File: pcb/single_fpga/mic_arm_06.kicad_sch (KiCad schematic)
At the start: 17 parts, among them U105 CDCLVC1108PW, U49 IM72D128V01XTMA1, U50 IM72D128V01XTMA1, U51 IM72D128V01XTMA1, U52 IM72D128V01XTMA1, U53 IM72D128V01XTMA1, U54 IM72D128V01XTMA1, U55 IM72D128V01XTMA1, U56 IM72D128V01XTMA1

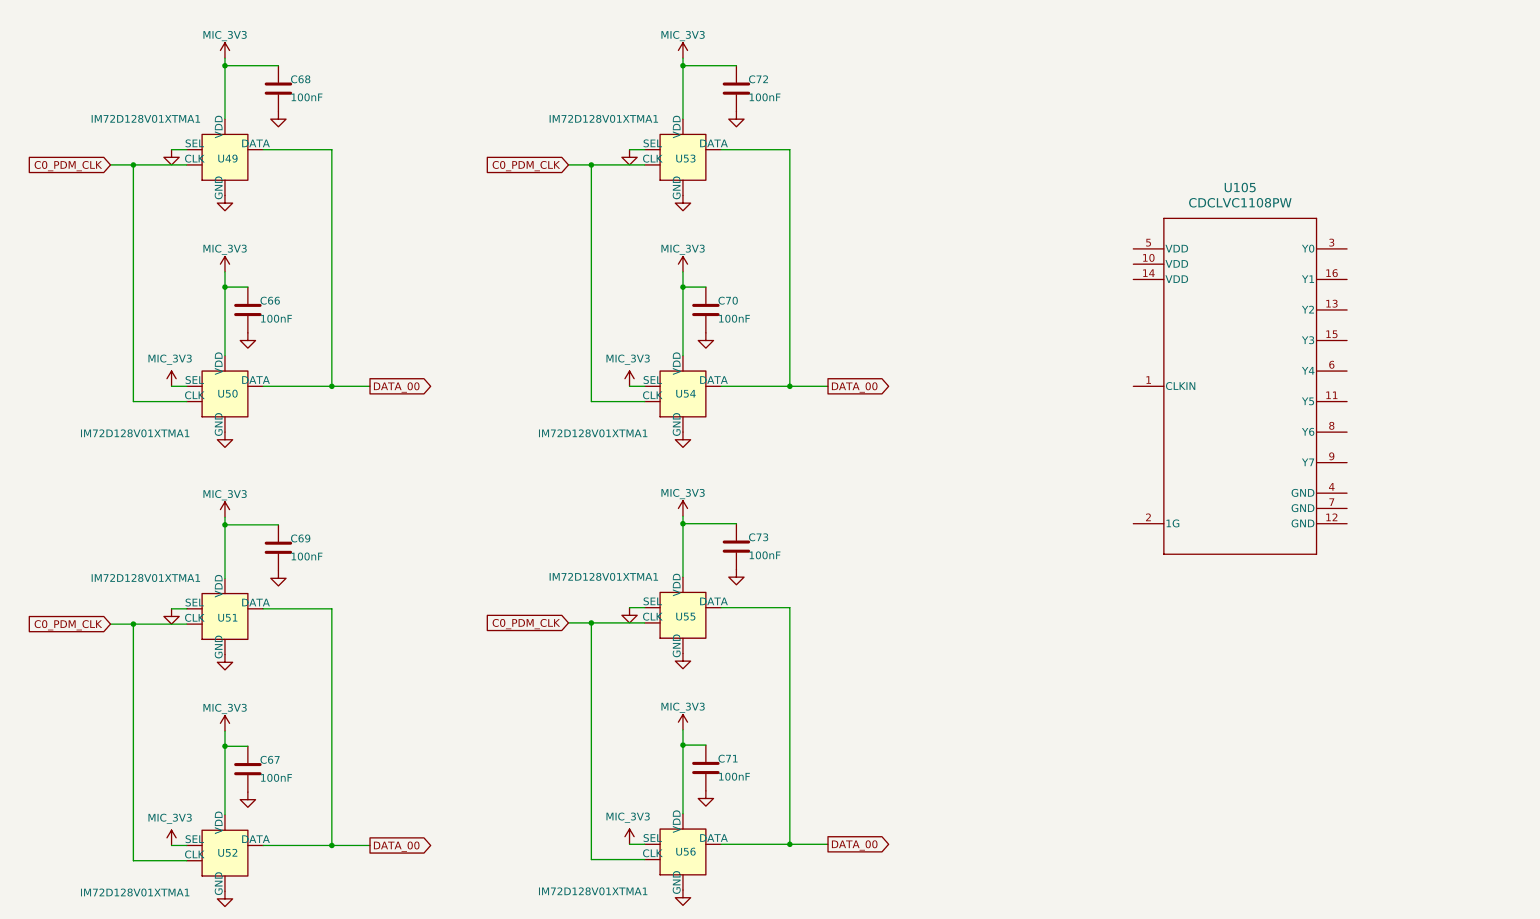
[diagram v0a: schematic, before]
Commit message: Fixed clocks and names.
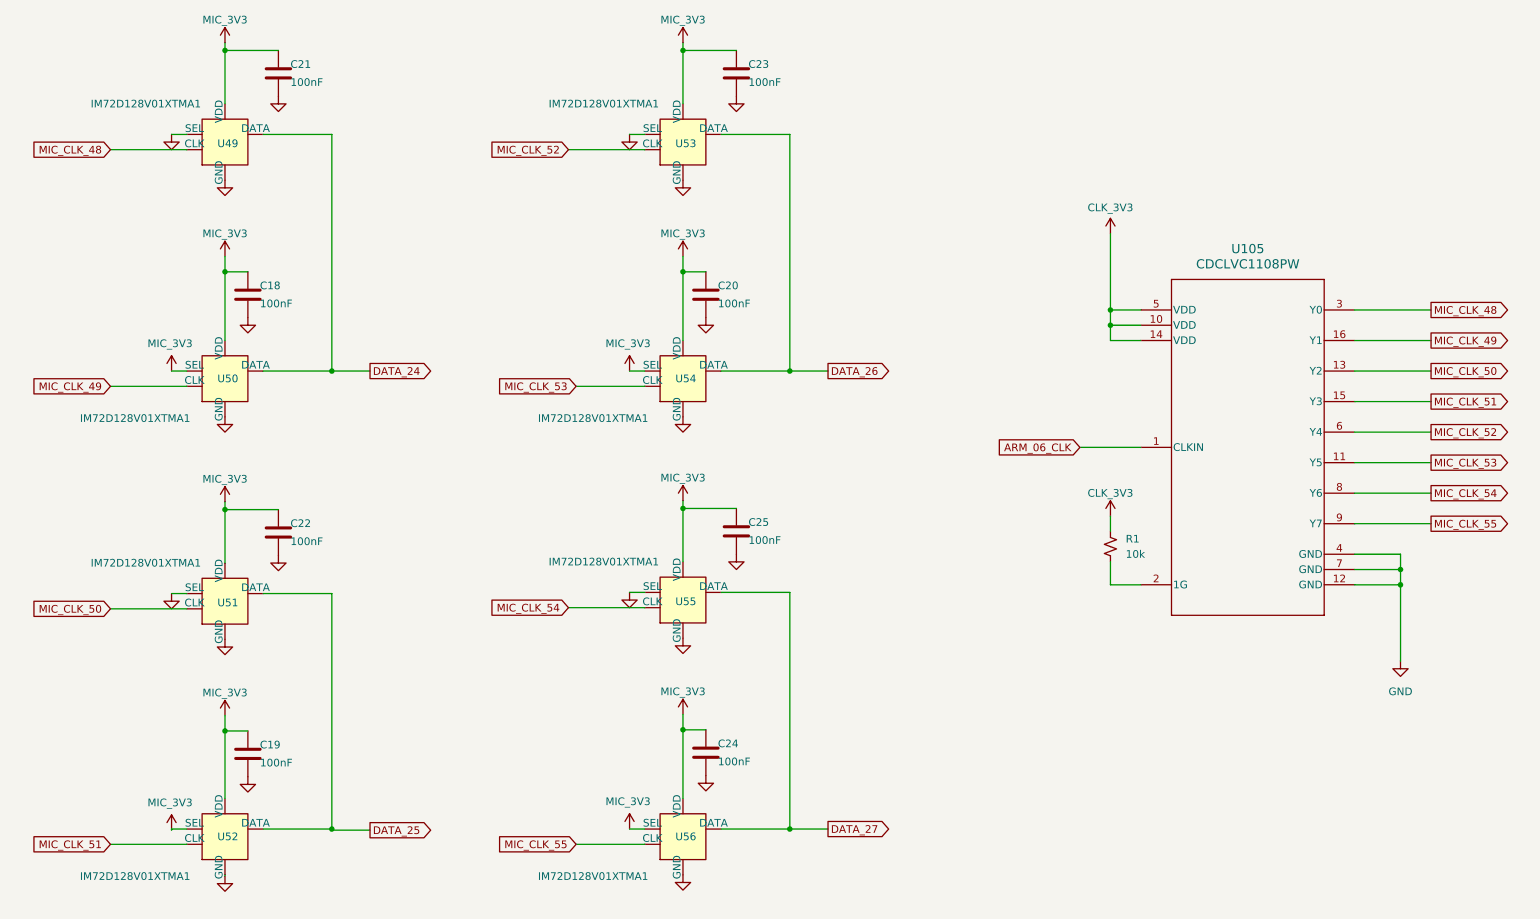
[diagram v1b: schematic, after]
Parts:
- removed C66, C67, C68, C69, C70, C71, C72, C73: 100nF, Capacitor_SMD:C_0603_1608Metric, symbol Device:C
- added C18, C19, C20, C21, C22, C23, C24, C25: 100nF, Capacitor_SMD:C_0603_1608Metric, symbol Device:C
- added R1: 10k, PCM_SparkFun-Resistor:R_0603_1608Metric, symbol PCM_SparkFun-Resistor:10k_0603
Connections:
- net GND: now also U105.12 (GND), U105.4 (GND), U105.7 (GND), C18.2, C19.2, C20.2, C21.2, C22.2, C23.2, C24.2, C25.2
- net MIC_3V3: now also C18.1, C19.1, C20.1, C21.1, C22.1, C23.1, C24.1, C25.1
- net ARM_06_CLK: now reaches U105.1 (CLKIN)
- net CLK_3V3: now reaches U105.10 (VDD)
- net CLK_3V3: now also U105.14 (VDD), U105.5 (VDD), R1.2
- net MIC_CLK_53: now reaches U105.11 (Y5)
- net MIC_CLK_53: now also U54.3 (CLK)
- net MIC_CLK_50: now reaches U105.13 (Y2)
- net MIC_CLK_50: now also U51.3 (CLK)
- net MIC_CLK_51: now reaches U105.15 (Y3)
- net MIC_CLK_51: now also U52.3 (CLK)
- net MIC_CLK_49: now reaches U105.16 (Y1)
- net MIC_CLK_49: now also U50.3 (CLK)
- net at U105.2 (1G): now also R1.1
- net MIC_CLK_48: now reaches U105.3 (Y0)
- net MIC_CLK_48: now also U49.3 (CLK)
- net MIC_CLK_52: now reaches U105.6 (Y4)
- net MIC_CLK_52: now also U53.3 (CLK)
- net MIC_CLK_54: now reaches U105.8 (Y6)
- net MIC_CLK_54: now also U55.3 (CLK)
- net MIC_CLK_55: now reaches U105.9 (Y7)
- net MIC_CLK_55: now also U56.3 (CLK)
- removed net C0_PDM_CLK: U49.3 (CLK), U50.3 (CLK), U51.3 (CLK), U52.3 (CLK), U53.3 (CLK), U54.3 (CLK), U55.3 (CLK), U56.3 (CLK)
- removed net DATA_00: U49.1 (DATA), U50.1 (DATA), U51.1 (DATA), U52.1 (DATA), U53.1 (DATA), U54.1 (DATA), U55.1 (DATA), U56.1 (DATA)
- new net DATA_24: U49.1 (DATA), U50.1 (DATA)
- new net DATA_25: U51.1 (DATA), U52.1 (DATA)
- new net DATA_26: U53.1 (DATA), U54.1 (DATA)
- new net DATA_27: U55.1 (DATA), U56.1 (DATA)

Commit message: Fixed all duplicate refdes's.
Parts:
- renumbered C18 to C66, C19 to C67, C20 to C68, C21 to C69, C22 to C70, C23 to C71, C24 to C72, C25 to C73, R1 to R11

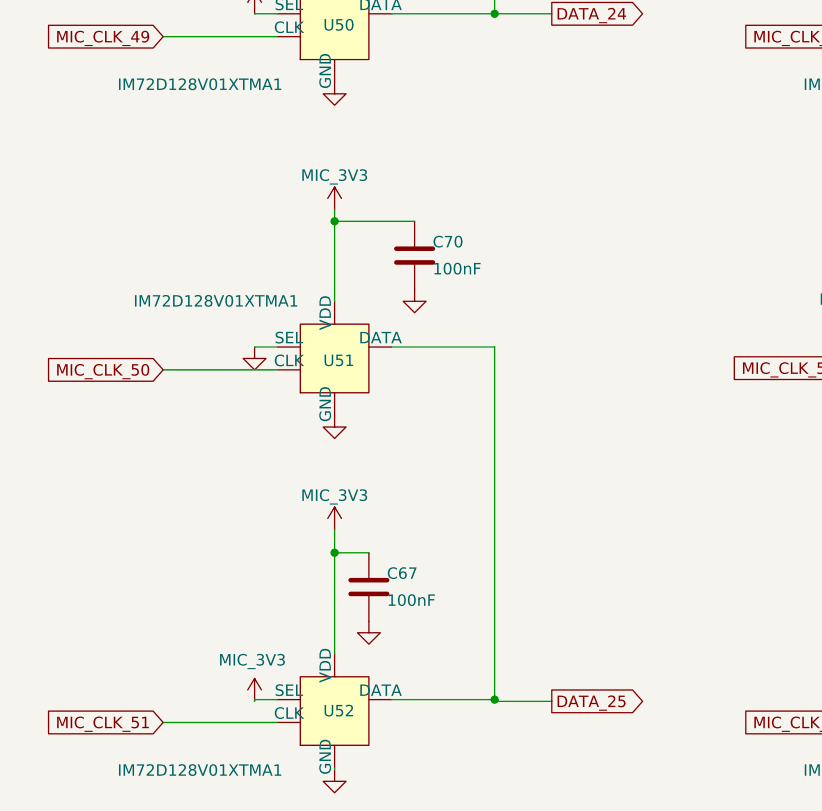
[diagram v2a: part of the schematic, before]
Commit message: Fixed symbol library references.
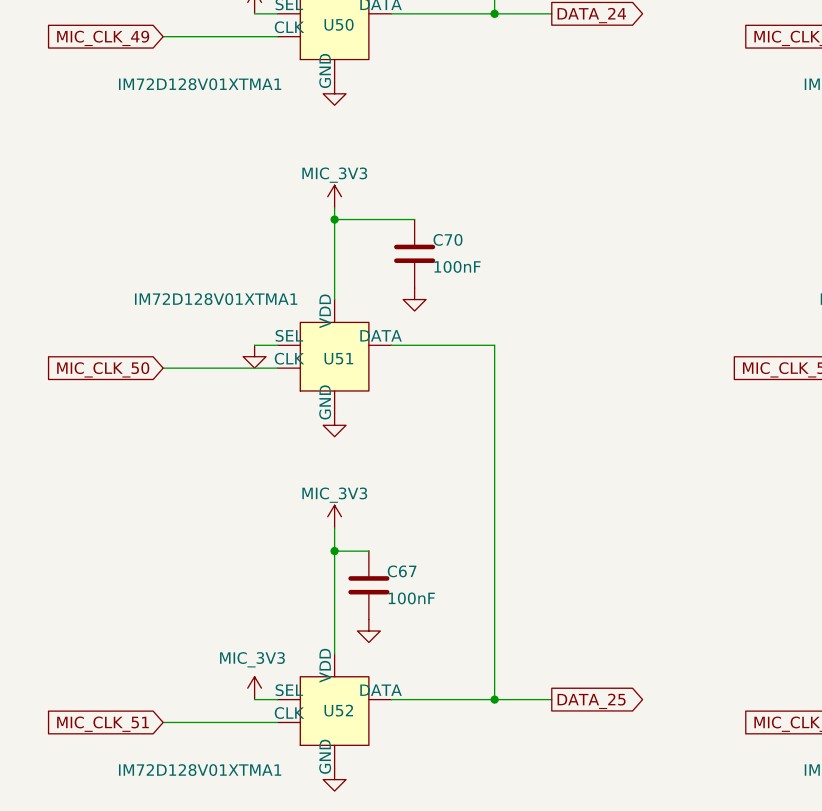
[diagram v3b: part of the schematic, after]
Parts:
- U105: footprint PW0016A_N -> CDCLVC1108:PW0016A_N

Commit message: Fixed footprints. Added missing mic. Relinked placed footprints.
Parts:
- U49, U50, U51, U52, U53, U54, U55, U56: footprint (none) -> IM72D128:IFX-PG-LLGA-5-4
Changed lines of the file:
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@@
 			)
 		)
-		(property "Footprint" ""
+		(property "Footprint" "IM72D128:IFX-PG-LLGA-5-4"
 			(at 59.69 160.02 0)
 			(hide yes)
@@
 			)
 		)
-		(property "Footprint" ""
+		(property "Footprint" "IM72D128:IFX-PG-LLGA-5-4"
 			(at 135.89 160.02 0)
 			(hide yes)
@@
 			)
 		)
-		(property "Footprint" ""
+		(property "Footprint" "IM72D128:IFX-PG-LLGA-5-4"
 			(at 59.69 83.82 0)
 			(hide yes)
@@
 			)
 		)
-		(property "Footprint" ""
+		(property "Footprint" "IM72D128:IFX-PG-LLGA-5-4"
 			(at 59.69 120.65 0)
 			(hide yes)
@@
 			)
 		)
-		(property "Footprint" ""
+		(property "Footprint" "IM72D128:IFX-PG-LLGA-5-4"
 			(at 59.69 44.45 0)
 			(hide yes)
@@
 			)
 		)
-		(property "Footprint" ""
+		(property "Footprint" "IM72D128:IFX-PG-LLGA-5-4"
 			(at 135.89 83.82 0)
 			(hide yes)
@@
 			)
 		)
-		(property "Footprint" ""
+		(property "Footprint" "IM72D128:IFX-PG-LLGA-5-4"
 			(at 135.89 44.45 0)
 			(hide yes)
@@
 			)
 		)
-		(property "Footprint" ""
+		(property "Footprint" "IM72D128:IFX-PG-LLGA-5-4"
 			(at 135.89 120.65 0)
 			(hide yes)

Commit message: Updated all refdes's.
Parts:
- removed C66, C67, C68, C69, C70, C71, C72, C73: 100nF, Capacitor_SMD:C_0603_1608Metric, symbol Device:C
- removed R11: 10k, PCM_SparkFun-Resistor:R_0603_1608Metric, symbol PCM_SparkFun-Resistor:10k_0603
- removed U105: CDCLVC1108PW, CDCLVC1108:PW0016A_N, symbol CDCLVC1108:CDCLVC1108PW
- removed U49, U50, U51, U52, U53, U54: IM72D128V01XTMA1, IM72D128:IFX-PG-LLGA-5-4, symbol multi_fpga:IM72D128
- added C49, C50, C51, C52, C53, C54, C55, C56: 100nF, Capacitor_SMD:C_0603_1608Metric, symbol Device:C
- added R7: 10k, PCM_SparkFun-Resistor:R_0603_1608Metric, symbol PCM_SparkFun-Resistor:10k_0603
- added U57, U58, U59, U60, U61, U62: IM72D128V01XTMA1, IM72D128:IFX-PG-LLGA-5-4, symbol multi_fpga:IM72D128
- added U63: CDCLVC1108PW, CDCLVC1108:PW0016A_N, symbol CDCLVC1108:CDCLVC1108PW
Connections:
- net ARM_06_CLK: now also U63.1 (CLKIN)
- net CLK_3V3: now also R7.2, U63.10 (VDD), U63.14 (VDD), U63.5 (VDD)
- net DATA_24: now also U55.1 (DATA), U56.1 (DATA)
- net DATA_25: now also U57.1 (DATA), U58.1 (DATA)
- net DATA_26: now also U59.1 (DATA), U60.1 (DATA)
- net DATA_27: now also U61.1 (DATA), U62.1 (DATA); no longer U55.1 (DATA), U56.1 (DATA)
- net GND: now also C49.2, C50.2, C51.2, C52.2, C53.2, C54.2, C55.2, C56.2, U57.4 (SEL), U57.5 (GND), U58.5 (GND), U59.4 (SEL), U59.5 (GND), U60.5 (GND), U61.4 (SEL), U61.5 (GND), U62.5 (GND), U63.12 (GND), U63.4 (GND), U63.7 (GND)
- net MIC_3V3: now also C49.1, C50.1, C51.1, C52.1, C53.1, C54.1, C55.1, C56.1, U57.2 (VDD), U58.2 (VDD), U58.4 (SEL), U59.2 (VDD), U60.2 (VDD), U60.4 (SEL), U61.2 (VDD), U62.2 (VDD), U62.4 (SEL)
- net MIC_CLK_48: now also U55.3 (CLK), U63.3 (Y0)
- net MIC_CLK_49: now also U56.3 (CLK), U63.16 (Y1)
- net MIC_CLK_50: now also U57.3 (CLK), U63.13 (Y2)
- net MIC_CLK_51: now also U58.3 (CLK), U63.15 (Y3)
- net MIC_CLK_52: now also U59.3 (CLK), U63.6 (Y4)
- net MIC_CLK_53: now also U60.3 (CLK), U63.11 (Y5)
- net MIC_CLK_54: now also U61.3 (CLK), U63.8 (Y6); no longer U55.3 (CLK)
- net MIC_CLK_55: now also U62.3 (CLK), U63.9 (Y7); no longer U56.3 (CLK)
- new net: R7.1, U63.2 (1G)
